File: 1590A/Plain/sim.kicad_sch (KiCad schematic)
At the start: 11 parts

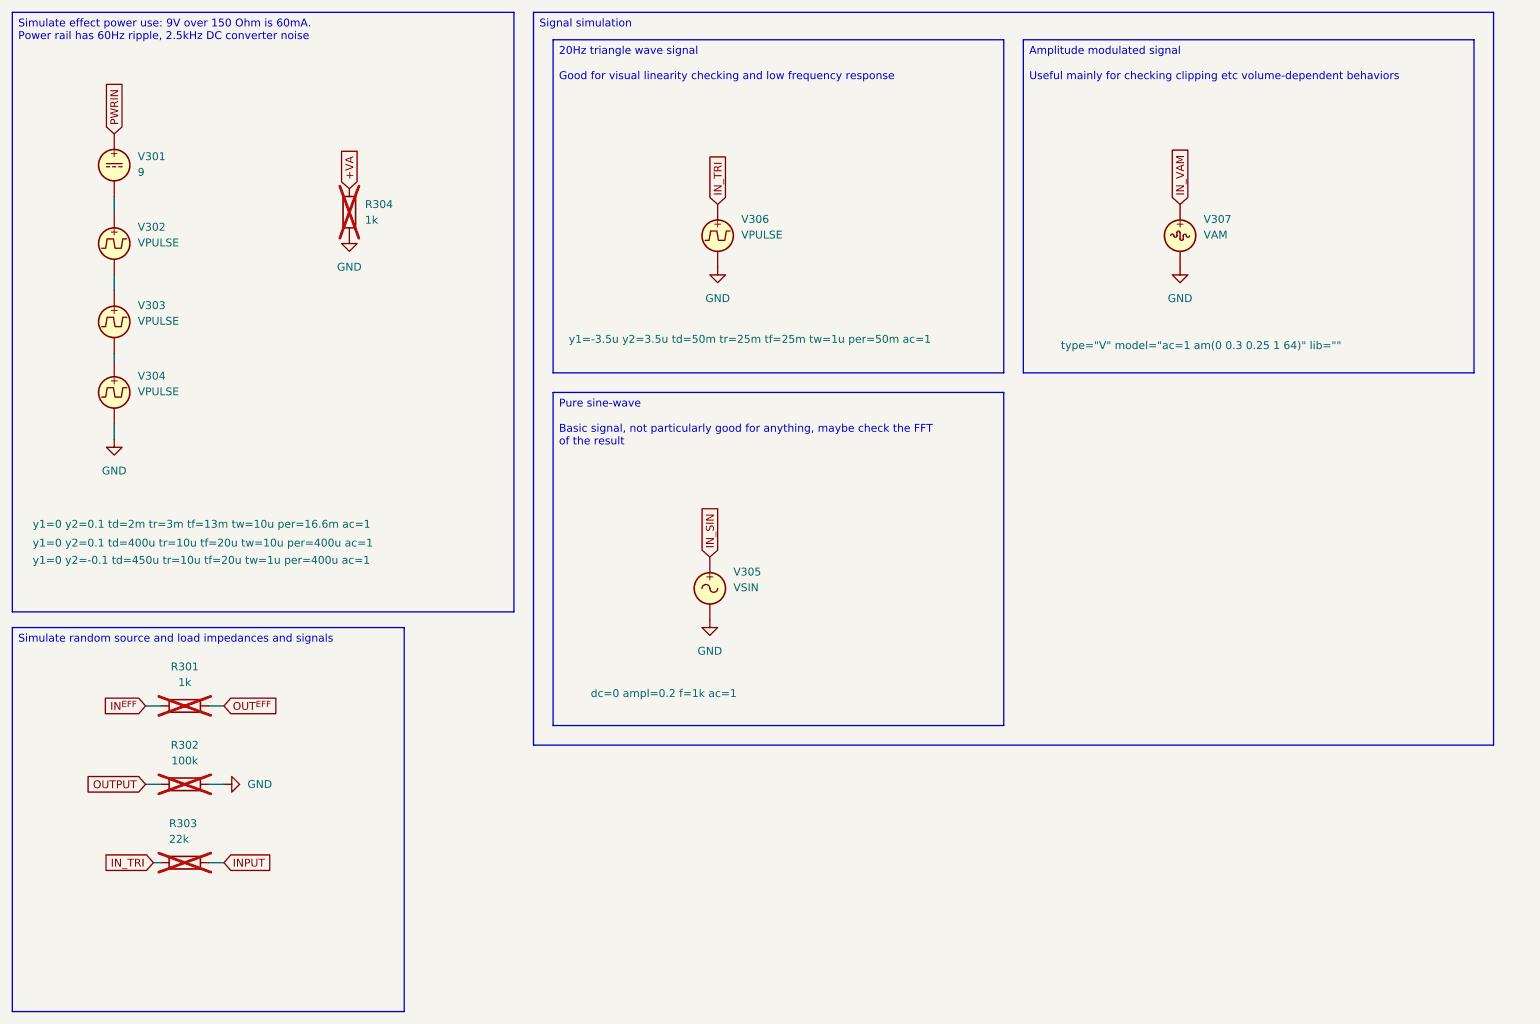
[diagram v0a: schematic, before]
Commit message: Update plain 1590A board
I had decided that the effect board didn't need the input to be
ground-biased, and that was very wrong, and made some of my old effect
boards not work.  So add the AC couple capacitor and resistor to ground.

Also do the same boring RC power smoothing with the voodoo ferrite for
the +VA line.  Let's keep it simple and realistic - the noise isn't some
60Hz ripple, it's all SMPS high-frequency stuff.

Signed-off-by: Linus Torvalds <torvalds@linux-foundation.org>
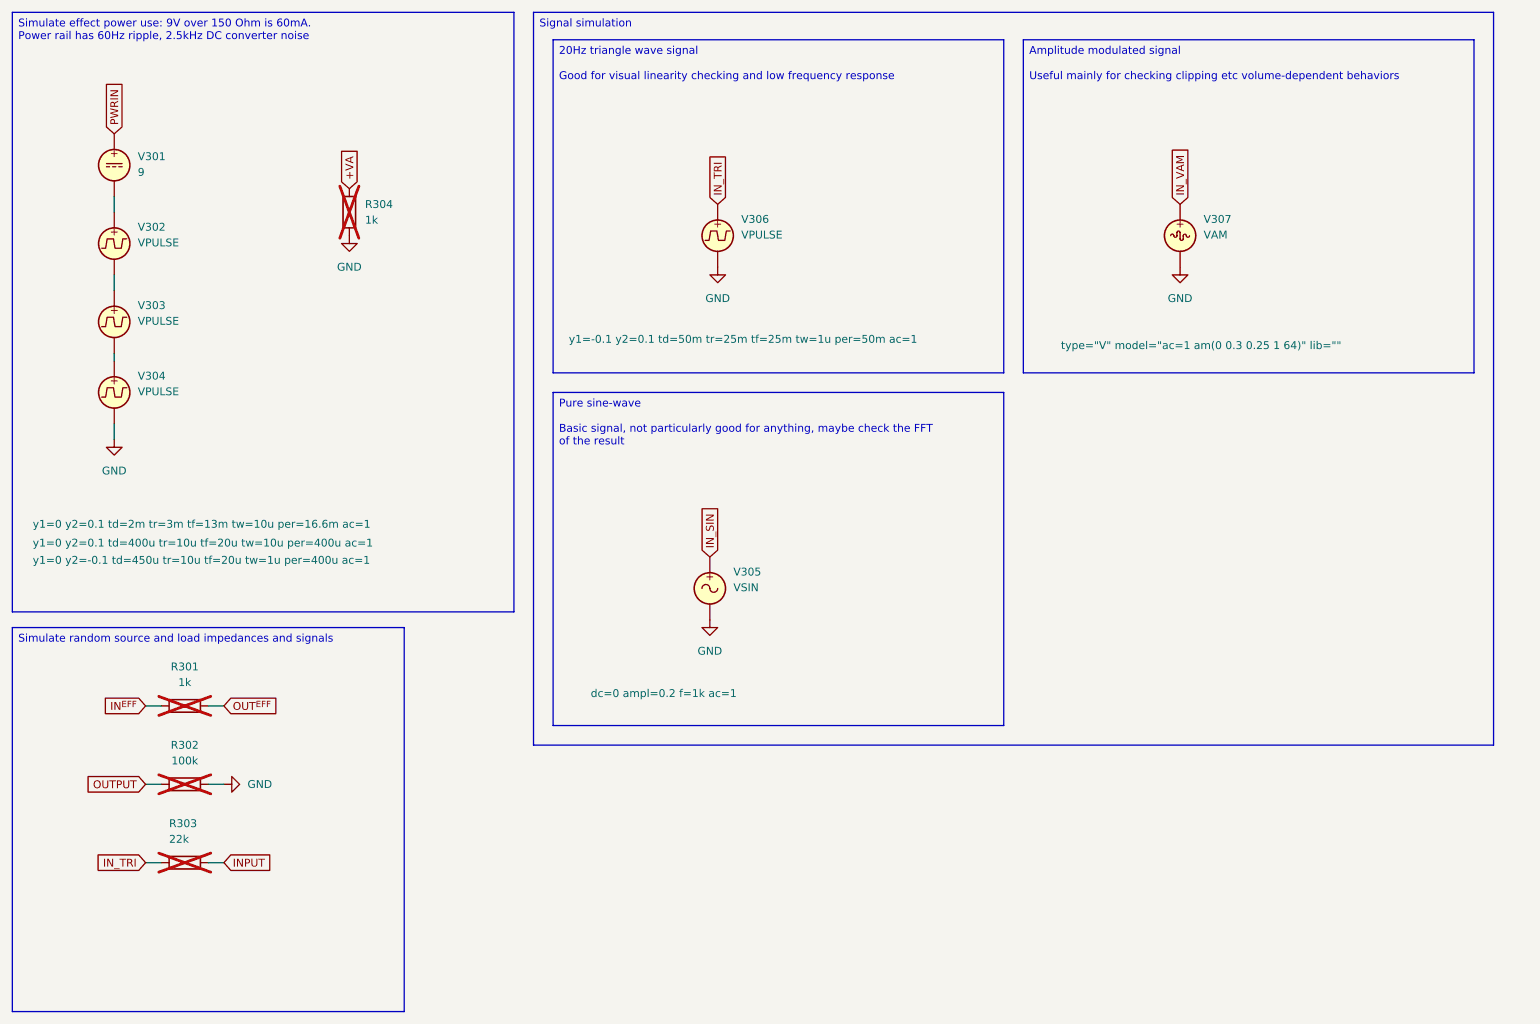
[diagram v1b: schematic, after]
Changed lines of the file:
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@@
 	(wire
 		(pts
-			(xy 38.1 152.4) (xy 36.83 152.4)
+			(xy 45.72 127) (xy 48.26 127)
 		)
 		(stroke
@@
 	(wire
 		(pts
-			(xy 45.72 127) (xy 48.26 127)
+			(xy 35.56 152.4) (xy 38.1 152.4)
 		)
 		(stroke
@@
 		)
 	)
-	(global_label "IN_TRI"
+	(global_label "+VA"
 		(shape input)
-		(at 36.83 152.4 180)
+		(at 68.58 43.18 90)
 		(fields_autoplaced yes)
 		(effects
@@
 				(size 1.27 1.27)
 			)
-			(justify right)
+			(justify left)
 		)
 		(property "Intersheetrefs" "${INTERSHEET_REFS}"
-			(at 28.0995 152.4 0)
-			(effects
-				(font
-					(size 1.27 1.27)
-				)
-				(justify right)
-				(hide yes)
-			)
-		)
-	)
-	(global_label "+VA"
+			(at 68.58 36.4452 90)
+			(effects
+				(font
+					(size 1.27 1.27)
+				)
+				(justify left)
+				(hide yes)
+			)
+		)
+	)
+	(global_label "IN^{EFF}"
 		(shape input)
-		(at 68.58 43.18 90)
+		(at 35.56 127 180)
 		(fields_autoplaced yes)
 		(effects
@@
 				(size 1.27 1.27)
 			)
-			(justify left)
+			(justify right)
 		)
 		(property "Intersheetrefs" "${INTERSHEET_REFS}"
-			(at 68.58 36.4452 90)
-			(effects
-				(font
-					(size 1.27 1.27)
-				)
-				(justify left)
-				(hide yes)
-			)
-		)
-	)
-	(global_label "IN^{EFF}"
+			(at 27.9277 127 0)
+			(effects
+				(font
+					(size 1.27 1.27)
+				)
+				(justify right)
+				(hide yes)
+			)
+		)
+	)
+	(global_label "IN_SIN"
 		(shape input)
-		(at 35.56 127 180)
+		(at 127 102.87 90)
 		(fields_autoplaced yes)
 		(effects
@@
 				(size 1.27 1.27)
 			)
-			(justify right)
+			(justify left)
 		)
 		(property "Intersheetrefs" "${INTERSHEET_REFS}"
-			(at 27.9277 127 0)
-			(effects
-				(font
-					(size 1.27 1.27)
-				)
-				(justify right)
-				(hide yes)
-			)
-		)
-	)
-	(global_label "IN_SIN"
+			(at 127 93.8371 90)
+			(effects
+				(font
+					(size 1.27 1.27)
+				)
+				(justify left)
+				(hide yes)
+			)
+		)
+	)
+	(global_label "INPUT"
 		(shape input)
-		(at 127 102.87 90)
+		(at 48.26 152.4 0)
 		(fields_autoplaced yes)
 		(effects
@@
 		)
 		(property "Intersheetrefs" "${INTERSHEET_REFS}"
-			(at 127 93.8371 90)
-			(effects
-				(font
-					(size 1.27 1.27)
-				)
-				(justify left)
-				(hide yes)
-			)
-		)
-	)
-	(global_label "INPUT"
+			(at 56.7486 152.4 0)
+			(effects
+				(font
+					(size 1.27 1.27)
+				)
+				(justify left)
+				(hide yes)
+			)
+		)
+	)
+	(global_label "IN_TRI"
 		(shape input)
-		(at 48.26 152.4 0)
+		(at 128.27 45.72 90)
 		(fields_autoplaced yes)
 		(effects
@@
 		)
 		(property "Intersheetrefs" "${INTERSHEET_REFS}"
-			(at 56.7486 152.4 0)
-			(effects
-				(font
-					(size 1.27 1.27)
-				)
-				(justify left)
-				(hide yes)
-			)
-		)
-	)
-	(global_label "IN_TRI"
+			(at 128.27 36.9895 90)
+			(effects
+				(font
+					(size 1.27 1.27)
+				)
+				(justify left)
+				(hide yes)
+			)
+		)
+	)
+	(global_label "PWRIN"
 		(shape input)
-		(at 128.27 45.72 90)
+		(at 30.48 34.29 90)
 		(fields_autoplaced yes)
 		(effects
@@
 		)
 		(property "Intersheetrefs" "${INTERSHEET_REFS}"
-			(at 128.27 36.9895 90)
-			(effects
-				(font
-					(size 1.27 1.27)
-				)
-				(justify left)
-				(hide yes)
-			)
-		)
-	)
-	(global_label "PWRIN"
+			(at 30.48 25.3781 90)
+			(effects
+				(font
+					(size 1.27 1.27)
+				)
+				(justify left)
+				(hide yes)
+			)
+		)
+	)
+	(global_label "IN_TRI"
 		(shape input)
-		(at 30.48 34.29 90)
+		(at 35.56 152.4 180)
 		(fields_autoplaced yes)
 		(effects
@@
 				(size 1.27 1.27)
 			)
-			(justify left)
+			(justify right)
 		)
 		(property "Intersheetrefs" "${INTERSHEET_REFS}"
-			(at 30.48 25.3781 90)
-			(effects
-				(font
-					(size 1.27 1.27)
-				)
-				(justify left)
+			(at 26.8295 152.4 0)
+			(effects
+				(font
+					(size 1.27 1.27)
+				)
+				(justify right)
 				(hide yes)
 			)
@@
 			)
 		)
-		(property "Sim.Params" "y1=-3.5u y2=3.5u td=50m tr=25m tf=25m tw=1u per=50m ac=1"
+		(property "Sim.Params" "y1=-0.1 y2=0.1 td=50m tr=25m tf=25m tw=1u per=50m ac=1"
 			(at 104.14 67.564 0)
 			(effects
